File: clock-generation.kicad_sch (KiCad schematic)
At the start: 28 parts, among them U1 Si5351B-B-GM, U2 TPS79301-EP, U3 DAC53002RTER, Y1 7M-27.000MEEQ-T

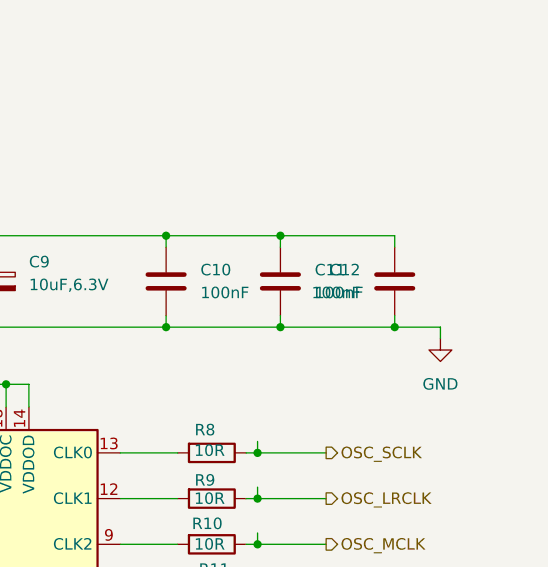
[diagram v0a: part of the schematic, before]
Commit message: minor DRC tweaks
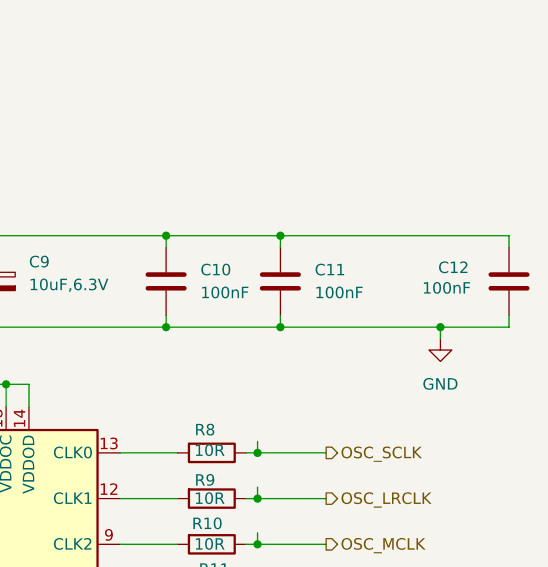
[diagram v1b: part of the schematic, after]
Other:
- moved on the sheet: C12
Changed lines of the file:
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@@
-	)
-	(junction
-		(at 242.57 78.74)
-		(diameter 0)
-		(color 0 0 0 0)
 	)
 	(junction
@@
 	(junction
 		(at 227.33 102.87)
+		(diameter 0)
+		(color 0 0 0 0)
+	)
+	(junction
+		(at 247.65 78.74)
 		(diameter 0)
 		(color 0 0 0 0)
@@
 	(wire
 		(pts
-			(xy 247.65 78.74) (xy 242.57 78.74)
-		)
-		(stroke
-			(width 0)
-			(type default)
-		)
-	)
-	(wire
-		(pts
 			(xy 217.17 68.58) (xy 217.17 69.85)
 		)
@@
 	(wire
 		(pts
+			(xy 255.27 78.74) (xy 247.65 78.74)
+		)
+		(stroke
+			(width 0)
+			(type default)
+		)
+	)
+	(wire
+		(pts
 			(xy 139.7 95.25) (xy 139.7 85.09)
 		)
@@
 	(wire
 		(pts
-			(xy 242.57 77.47) (xy 242.57 78.74)
+			(xy 255.27 77.47) (xy 255.27 78.74)
 		)
 		(stroke
@@
 	(wire
 		(pts
-			(xy 242.57 68.58) (xy 242.57 69.85)
+			(xy 255.27 68.58) (xy 255.27 69.85)
 		)
 		(stroke
@@
 	(wire
 		(pts
-			(xy 242.57 78.74) (xy 229.87 78.74)
+			(xy 229.87 78.74) (xy 247.65 78.74)
 		)
 		(stroke
@@
 	(wire
 		(pts
-			(xy 229.87 68.58) (xy 242.57 68.58)
+			(xy 229.87 68.58) (xy 255.27 68.58)
 		)
 		(stroke
@@
 	(symbol
 		(lib_id "Device:C")
-		(at 242.57 73.66 0)
-		(mirror y)
+		(at 255.27 73.66 0)
 		(unit 1)
 		(exclude_from_sim no)
@@
 		(dnp no)
 		(property "Reference" "C12"
-			(at 238.76 72.3899 0)
+			(at 247.396 72.136 0)
 			(effects
 				(font
@@
 		)
 		(property "Value" "100nF"
-			(at 238.76 74.9299 0)
+			(at 245.618 74.422 0)
 			(effects
 				(font
@@
 		)
 		(property "Footprint" "Capacitor_SMD:C_0603_1608Metric"
-			(at 241.6048 77.47 0)
+			(at 256.2352 77.47 0)
 			(effects
 				(font
@@
 		)
 		(property "Datasheet" "~"
-			(at 242.57 73.66 0)
+			(at 255.27 73.66 0)
 			(effects
 				(font
@@
 		)
 		(property "Description" "Unpolarized capacitor"
-			(at 242.57 73.66 0)
-			(effects
-				(font
+			(at 255.27 73.66 0)
+			(effects
+				(font

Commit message: Back-annotate BOM from CircuitHub
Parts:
- C1, C7: MPN (none) -> CC0603KRX7R9BB103; Manufacturer (none) -> Yageo
- C10, C11, C12, C2, C4: MPN (none) -> CC0603KRX7R8BB104; Manufacturer (none) -> Yageo
- C3: MPN (none) -> CC1206KKX7R6BB155; Manufacturer (none) -> Yageo
- C5, C8: MPN (none) -> CC0603KRX7R7BB105; Manufacturer (none) -> Yageo
- C6: MPN (none) -> CC0603JRNPO9BN150; Manufacturer (none) -> Yageo
- C9: MPN (none) -> CC0603MRX5R7BB106; Manufacturer (none) -> Yageo
- R1: MPN (none) -> PTN0603Y5000BST1; Manufacturer (none) -> Vishay
- R10, R11, R8, R9: MPN (none) -> CRCW060310R0JNEA; Manufacturer (none) -> Vishay
- R2: MPN (none) -> CRCW0603100KFKEA; Manufacturer (none) -> Vishay
- R3: MPN (none) -> CRCW060328K0FKEA; Manufacturer (none) -> Vishay
- R4, R5: MPN (none) -> CRCW060310K0FKEA; Manufacturer (none) -> Vishay
- R6: MPN (none) -> CRCW060351K1FKEA; Manufacturer (none) -> Vishay
- R7: MPN (none) -> CRCW060330K1FKEA; Manufacturer (none) -> Vishay
- U1: MPN (none) -> SI5351B-B-GM; Manufacturer (none) -> Skyworks Solutions
- U2: MPN (none) -> TPS79301DBVREP; Manufacturer (none) -> Texas Instruments
- U3: MPN (none) -> DAC53002RTER; Manufacturer (none) -> Texas Instruments
- Y1: MPN (none) -> 7M-27.000MEEQ-T; Manufacturer (none) -> TXC

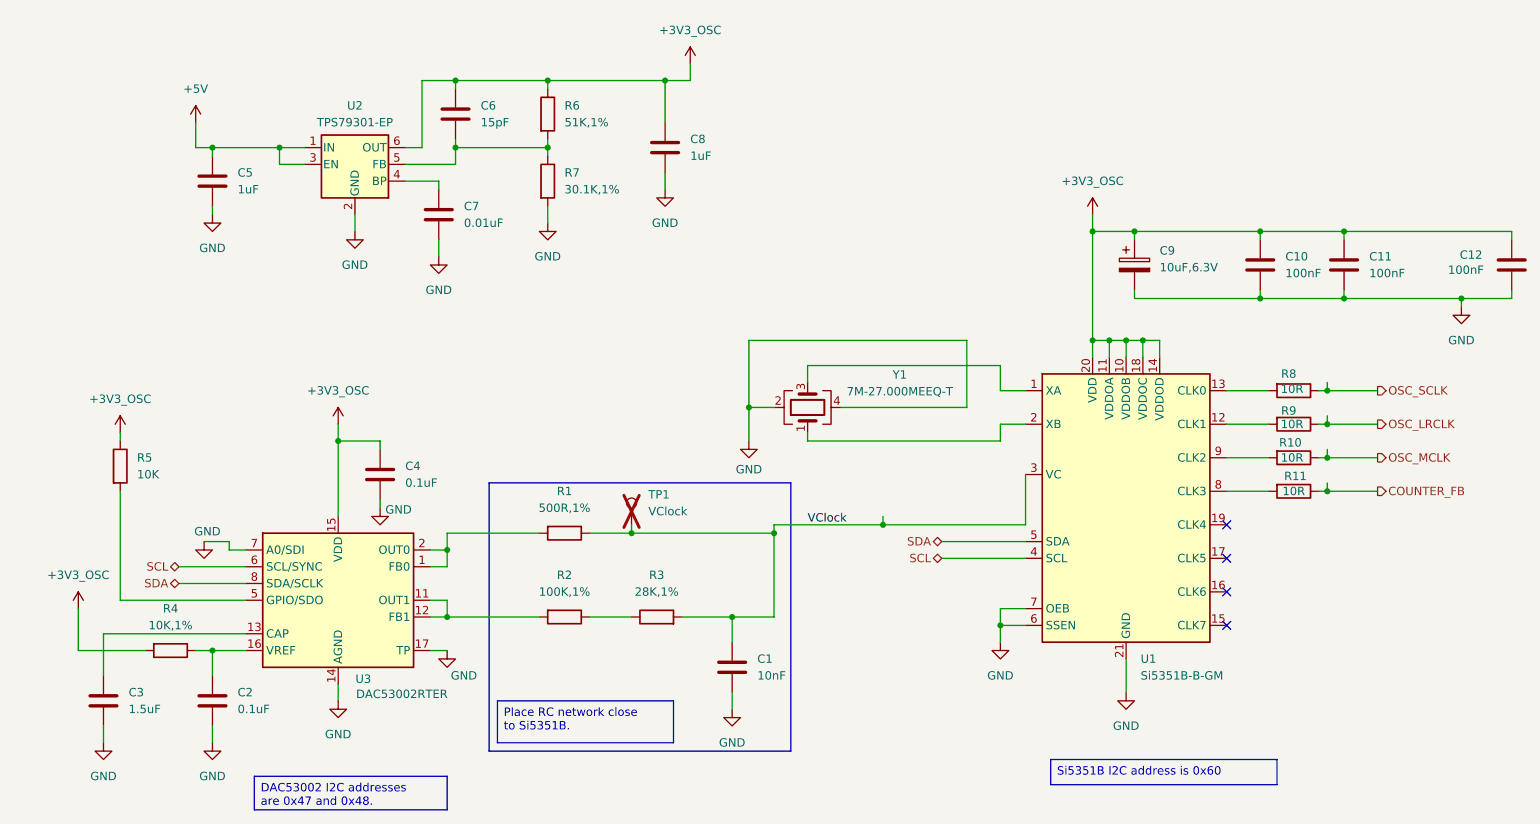
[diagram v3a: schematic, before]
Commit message: Added leds on Power and Mux sel lines per issues 12 and 15
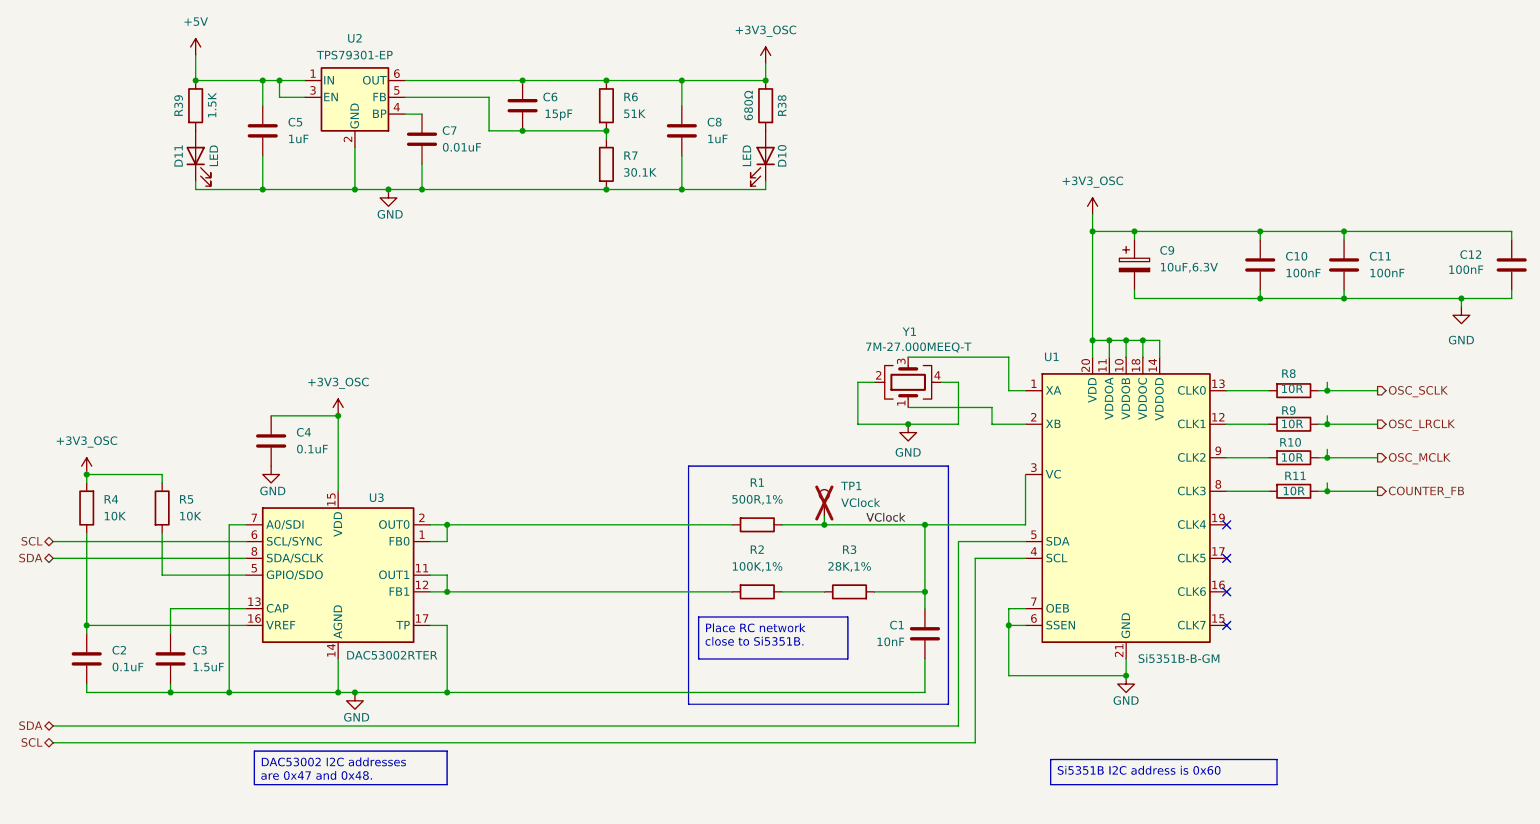
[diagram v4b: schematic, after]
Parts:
- added D10, D11: LED, LED_SMD:LED_0603_1608Metric_Pad1.05x0.95mm_HandSolder, symbol Device:LED
- added R38: 680Ω, Resistor_SMD:R_0603_1608Metric, symbol Device:R
- added R39: 1.5K, Resistor_SMD:R_0603_1608Metric, symbol Device:R
- R4: value 10K,1% -> 10K
- R6: value 51K,1% -> 51K
- R7: value 30.1K,1% -> 30.1K
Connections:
- net +3V3_OSC: now also R38.1
- net +5V: now also R39.1
- net GND: now also D10.1 (K), D11.1 (K)
- new net: D10.2 (A), R38.2
- new net: D11.2 (A), R39.2
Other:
- moved on the sheet: C1, C2, C3, C4, C5, C6, C7, C8, R1, R2, R3, R4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

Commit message: Changed codec rail to 3V3_Osc and addressed all DRCs (including previous overrides)
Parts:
- U3: footprint Library:IC_BQ25306RTER -> Package_DFN_QFN:WQFN-16-1EP_3x3mm_P0.5mm_EP1.68x1.68mm_ThermalVias
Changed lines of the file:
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@@
 			)
 		)
-		(property "Footprint" "Library:IC_BQ25306RTER"
+		(property "Footprint" "Package_DFN_QFN:WQFN-16-1EP_3x3mm_P0.5mm_EP1.68x1.68mm_ThermalVias"
 			(at 66.04 110.49 0)
 			(effects
